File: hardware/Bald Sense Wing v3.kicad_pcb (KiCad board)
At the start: 4 copper layers, 50.8 x 22.9 mm, 53 parts, among them J1 feather long, J2 feather short, J3 1140084168, J4 STEMMA-QT, Q1 Q_PNP_BEC, Q2 Q_NPN_BEC, SW1 PTS810, U1 APDS-9960, U2 DS3231MZ, U3 SHT30-DIS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

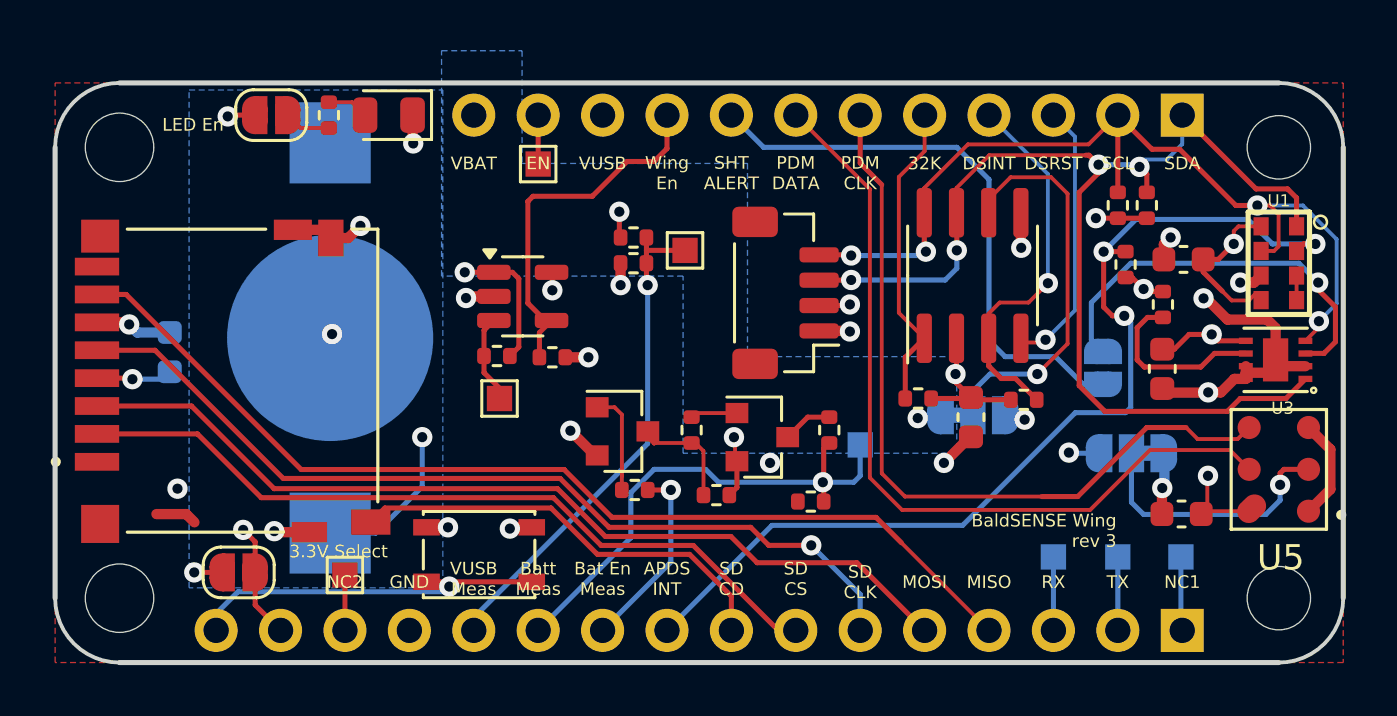
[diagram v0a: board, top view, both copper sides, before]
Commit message: Cleaned up power rails. Prepping for Macrofab DRC
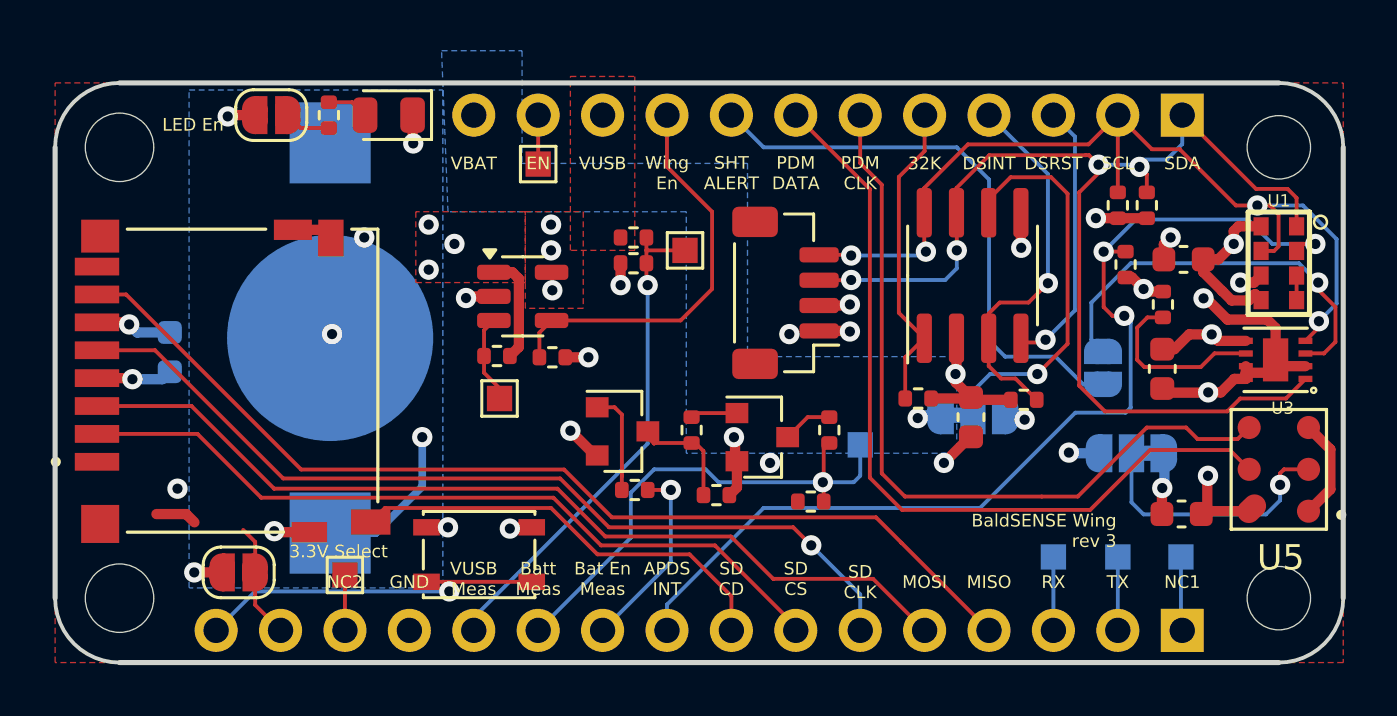
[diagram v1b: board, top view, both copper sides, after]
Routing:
- net +3v3_Feather: track 23.0 -> 5.30 mm, vias 2 -> 3
- net +Vusb: track 5.12 -> 0.07 mm, vias 1 -> 0
- net /Load_SW_En: track 14.6 -> 16.1 mm
- net GND: track 39.7 -> 38.3 mm, vias 21 -> 22
- net +3.3V: track 36.3 -> 35.2 mm, vias 12 -> 14
- net /APDS_INT: track 39.8 -> 40.4 mm
- added copper zone on F.Cu, net +3.3V
- added copper zone on F.Cu, net +3v3_Feather
- added copper zone on In2.Cu, net +3v3_Feather
- added copper zone on F.Cu, net +Vusb

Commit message: updated custom footprints with (local) 3d models. ready for fab.
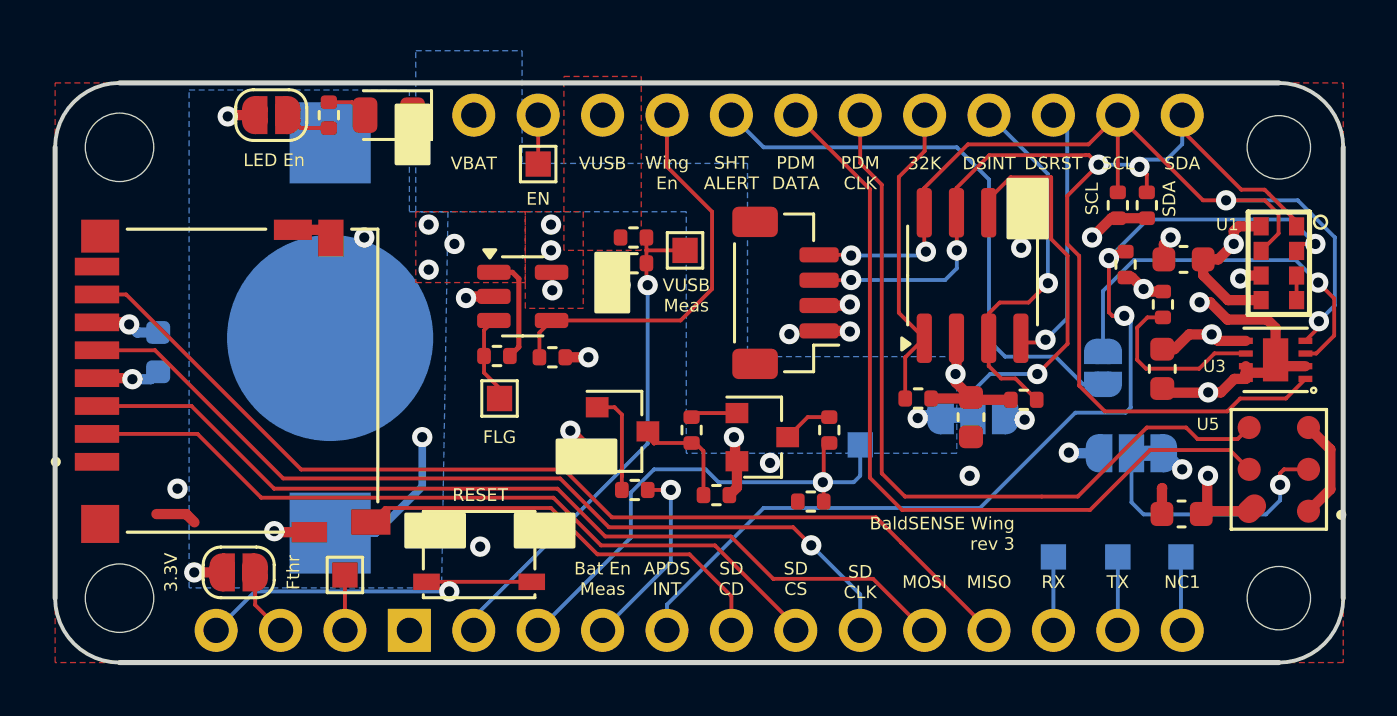
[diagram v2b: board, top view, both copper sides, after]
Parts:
- JP1: value 3.3V Select -> 3.3V
- SW1: footprint Button_Switch_SMD:SW_SPST_PTS810 -> My Libraries:SW_SPST_PTS810_with_3D
- moved C7 0.46 mm to (29.5, 36.0)
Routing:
- net GND: track 38.3 -> 34.2 mm, vias 22 -> 20
- net +3v3_Feather: track 5.30 -> 3.42 mm
- net /SCL: track 36.9 -> 37.8 mm
- net /APDS_INT: track 40.4 -> 39.8 mm
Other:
- rule solder_mask_min_width: 0.25 -> 0.1524
- board text added: "3v3"
- board text added: "BaldEE"
- board text added: "FLG"
- board text added: "Fthr"
- board text added: "RESET"
- board text added: "SHT30 Alert"
- board text removed: "NC2"
- board text removed: "Remove Silks Add Something fun on the power layer Add Silk for I2C Add Silk for Jumpers"
